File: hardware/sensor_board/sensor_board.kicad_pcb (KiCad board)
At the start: 2 copper layers, 24 x 28 mm, 10 parts, among them J0 Conn_01x04, U0 HIHxx3x-021, U1 MPL115A2, U2 P82B96

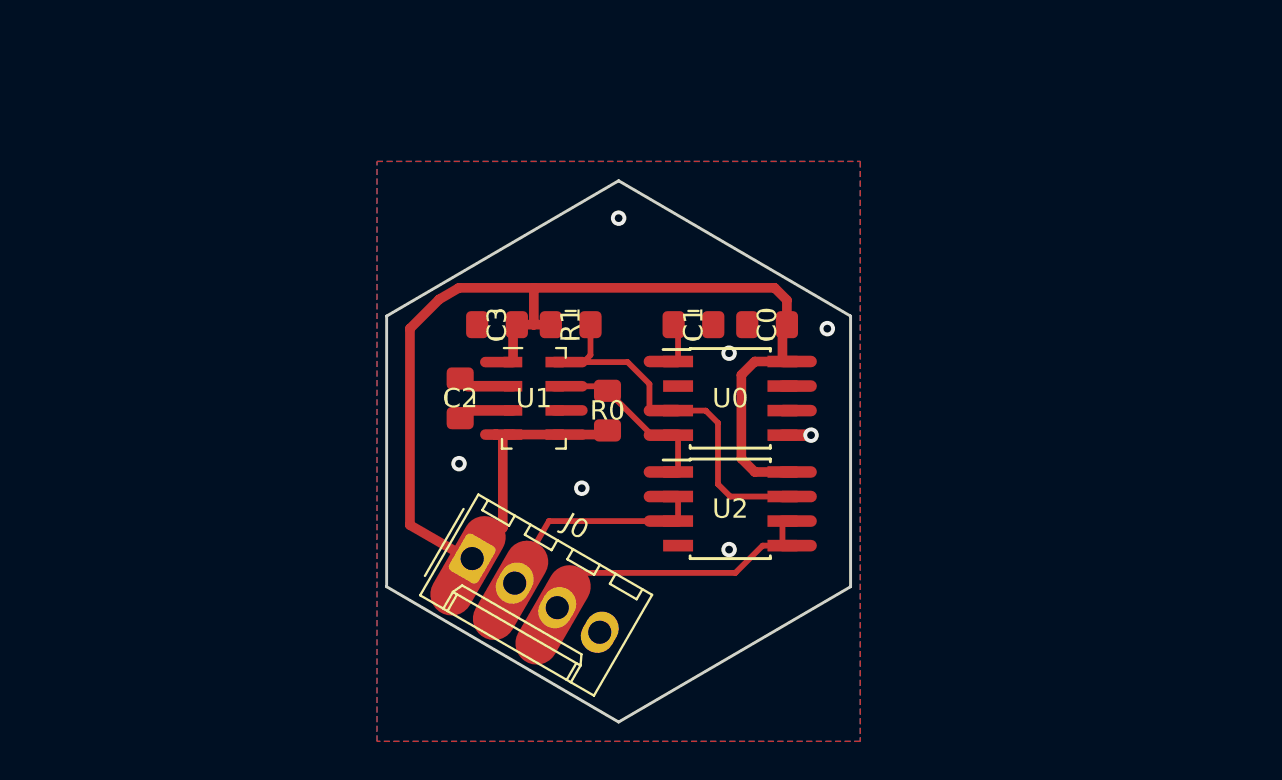
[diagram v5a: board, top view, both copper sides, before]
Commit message: Rework of sensor board and correction of pHAT
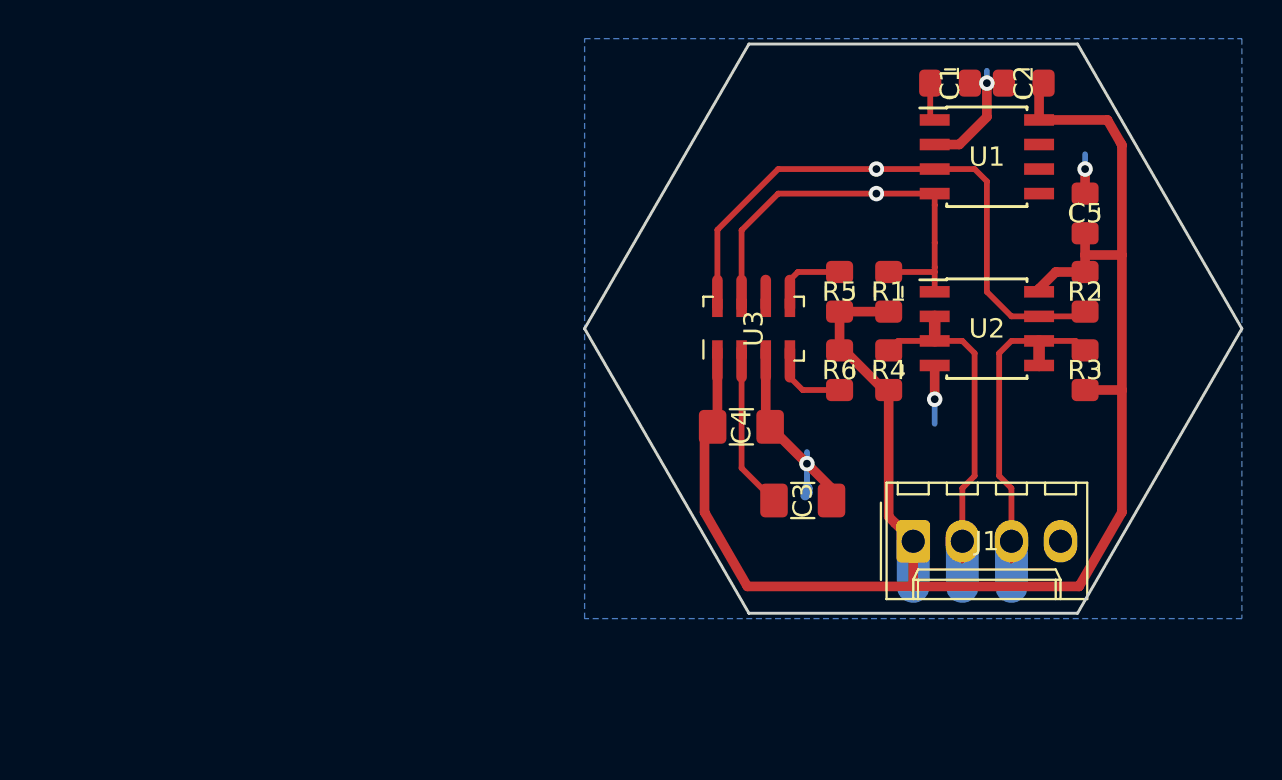
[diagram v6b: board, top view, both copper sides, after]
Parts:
- removed C0: 0.22µ, Capacitor_SMD:C_0805_2012Metric_Pad1.15x1.40mm_HandSolder
- removed J0: Conn_01x04, Connector_Molex:Molex_KK-254_AE-6410-04A_1x04_P2.54mm_Vertical
- removed R0: R, Resistor_SMD:R_0805_2012Metric_Pad1.15x1.40mm_HandSolder
- removed U0: HIHxx3x-021, Package_SO:SOIC-8_3.9x4.9mm_P1.27mm
- added C4: 1µ, Capacitor_SMD:C_1206_3216Metric_Pad1.42x1.75mm_HandSolder, F.Cu at (147.3, 88.7)
- added C5: 100n, Capacitor_SMD:C_0805_2012Metric_Pad1.15x1.40mm_HandSolder, F.Cu at (165.1, 77.7)
- added J1: Conn_01x04, Connector_Molex:Molex_KK-254_AE-6410-04A_1x04_P2.54mm_Vertical, F.Cu at (156.2, 94.7)
- added R2: R, Resistor_SMD:R_0805_2012Metric_Pad1.15x1.40mm_HandSolder, F.Cu at (165.1, 81.7)
- added R3: R, Resistor_SMD:R_0805_2012Metric_Pad1.15x1.40mm_HandSolder, F.Cu at (165.1, 85.8)
- added R4: R, Resistor_SMD:R_0805_2012Metric_Pad1.15x1.40mm_HandSolder, F.Cu at (155.0, 85.8)
- added R5: R, Resistor_SMD:R_0805_2012Metric_Pad1.15x1.40mm_HandSolder, F.Cu at (152.4, 81.7)
- added R6: R, Resistor_SMD:R_0805_2012Metric_Pad1.15x1.40mm_HandSolder, F.Cu at (152.4, 85.8)
- added U3: MPL115A2, Package_LGA:LGA-8_3x5mm_P1.25mm, F.Cu at (148.0, 83.7)
- C2: value 1µ -> 0.22µ
- C3: footprint Capacitor_SMD:C_0805_2012Metric_Pad1.15x1.40mm_HandSolder -> Capacitor_SMD:C_1206_3216Metric_Pad1.42x1.75mm_HandSolder
- U1: value MPL115A2 -> HIHxx3x-021; footprint Package_LGA:LGA-8_3x5mm_P1.25mm -> Package_SO:SOIC-8_3.9x4.9mm_P1.27mm
- moved C2 33.4 mm to (162.0, 71.0), turned to 180 degrees
- moved U1 26.6 mm to (160.1, 74.8)
- moved C3 18.2 mm to (150.5, 92.5), turned to 0 degrees
- moved C1 18.2 mm to (158.1, 71.0)
- moved R1 16.5 mm to (155.0, 81.7), turned to 90 degrees
- moved U2 16.2 mm to (160.1, 83.7)
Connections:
- C2 pad 1: Net-(C2-Pad1) -> +3V3
- C3 pad 1: +3V3 -> Net-(C3-Pad1)
- R1 pad 2: /SCL -> /SDA
- U1 pad 1: +3V3 -> /Vcore
- U1 pad 2: Net-(C2-Pad1) -> GND
- U1 pad 3: GND -> /SCL
- U1 pad 4: +3V3 -> /SDA
- U1 pad 5: +3V3 -> /alarm
- U1 pad 7: /SDA -> Net-(U1-Pad7)
- U1 pad 8: /SCL -> +3V3
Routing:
- net GND: track 2.90 -> 26.0 mm, vias 6 -> 4
- net +3V3: track 74.1 -> 90.3 mm
- net /SCL: track 21.7 -> 31.4 mm, vias 0 -> 1
- net /SDA: track 12.8 -> 22.2 mm, vias 0 -> 1
- net Net-(C3-Pad1): track 0.00 -> 8.51 mm
- net /SCL_ext: track 14.7 -> 19.5 mm
- net Net-(R6-Pad1): track 0.00 -> 4.28 mm
- net Net-(R5-Pad1): track 0.00 -> 4.18 mm
- net Net-(C2-Pad1): track 2.90 -> 0.00 mm
- net Net-(U0-Pad7): track 1.48 -> 0.00 mm
- net Net-(U0-Pad6): track 1.48 -> 0.00 mm
- net /alarm: track 1.48 -> 0.00 mm, vias 1 -> 0
- net /Vcore: track 3.48 -> 2.00 mm
- net Net-(U3-Pad6): track 0.00 -> 1.44 mm
- net Net-(U1-Pad6): track 1.44 -> 0.00 mm
- removed copper zone on F.Cu, net GND
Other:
- board size 24 x 28 mm -> 34 x 29.4 mm
